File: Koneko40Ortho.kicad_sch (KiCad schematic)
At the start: 24 parts, among them J1 Conn_01x04_MountingPin, J2 TC2030_SWD, SW73 SW_Push, U2 STM32L443CCUx, U4 3.3V Fixed Regulator

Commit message: Aug202023-7:30pm
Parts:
- added JP1: Jumper_2_Open, Connector_PinHeader_1.27mm:PinHeader_1x02_P1.27mm_Vertical, symbol Jumper:Jumper_2_Open
- added R1: 10k 0402, Resistor_SMD:R_0402_1005Metric, symbol Device:R_Small_US
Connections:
- net +3.3V: now also JP1.2 (B)
- net GND: now also R1.2
- net at U2.44 (PH3): now also JP1.1 (A), R1.1

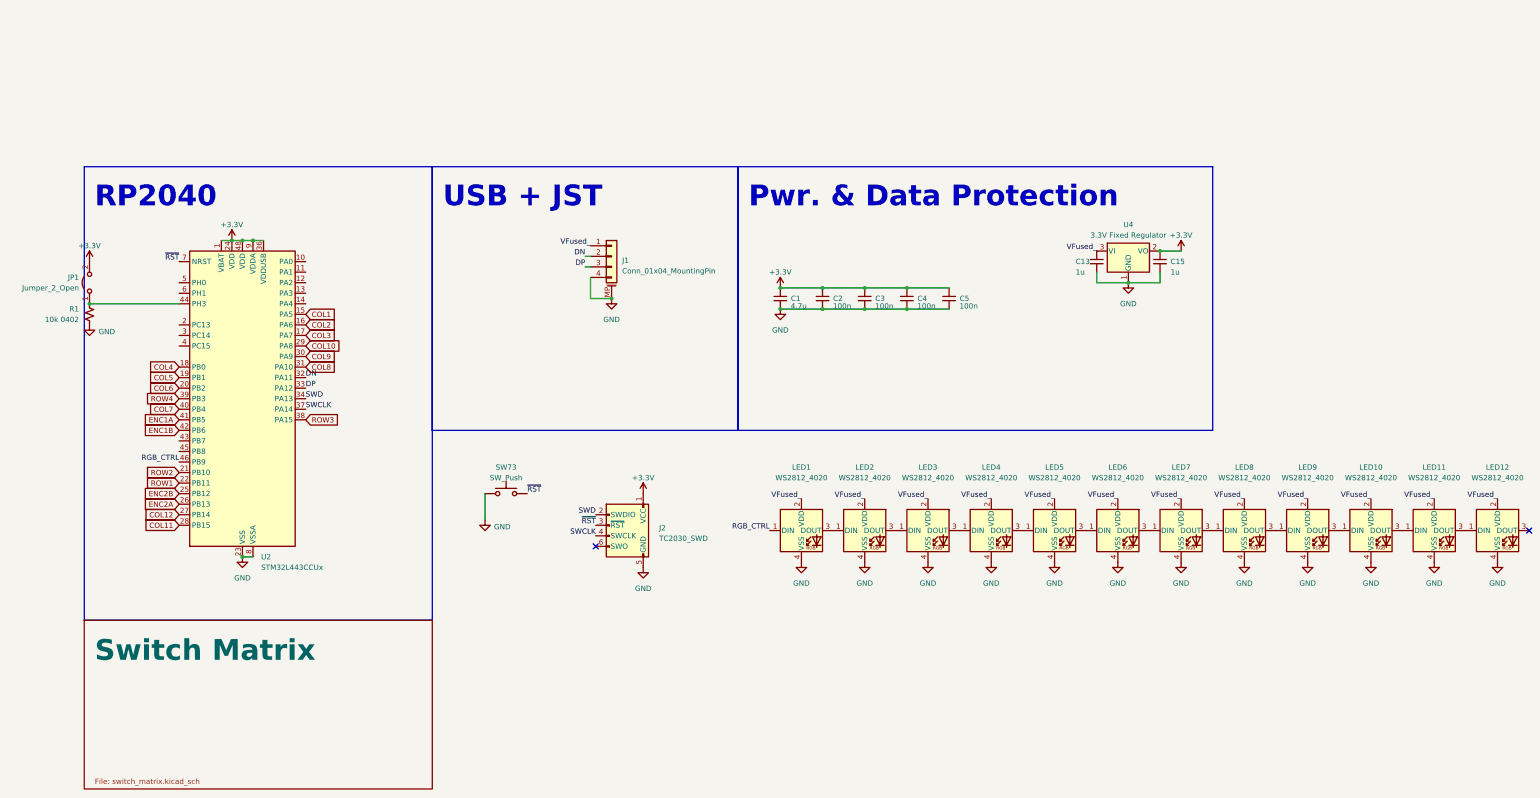
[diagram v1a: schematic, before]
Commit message: Refactored to use RP2040
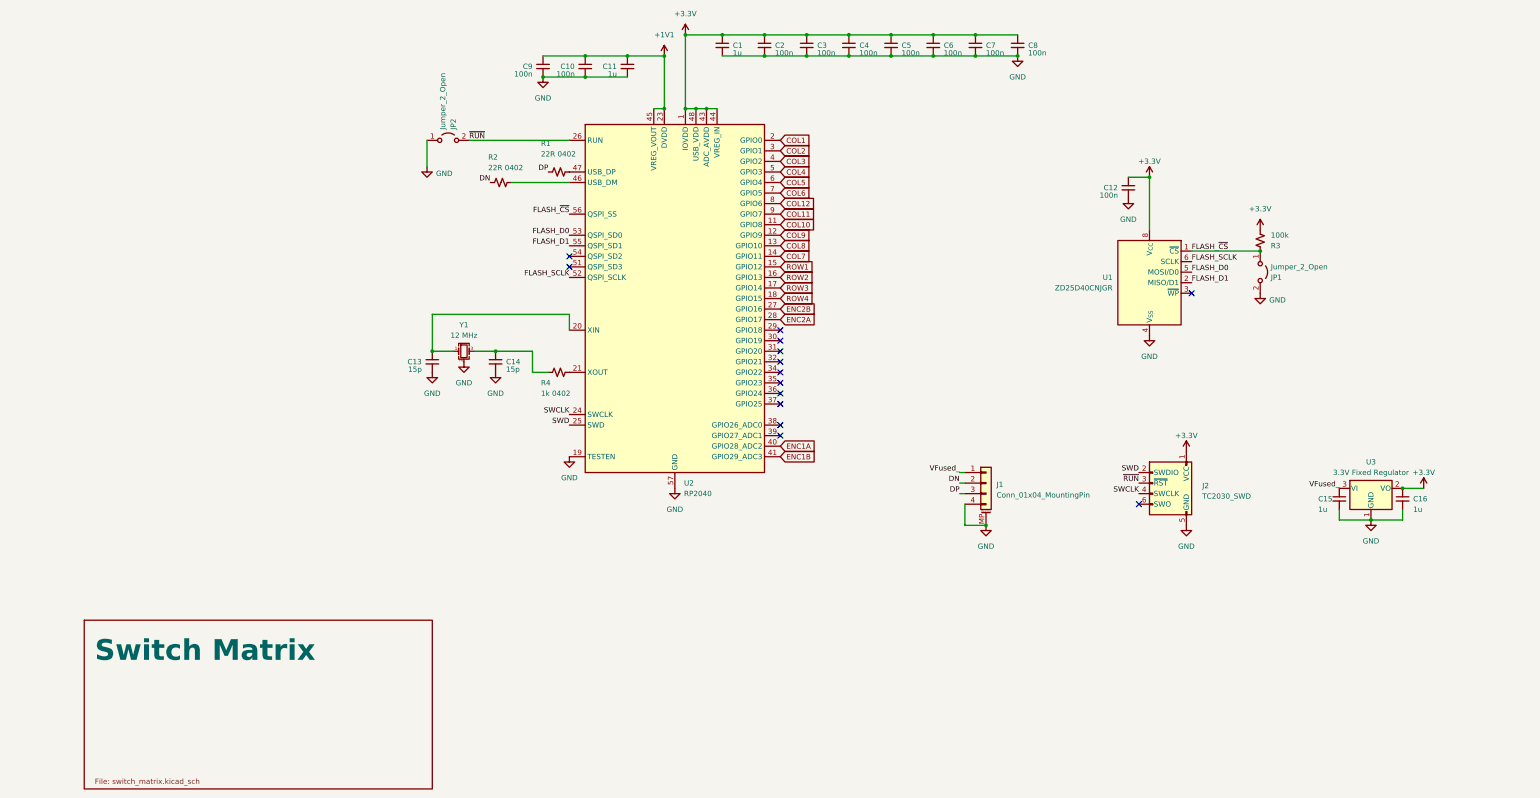
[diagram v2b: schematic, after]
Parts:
- removed LED1, LED10, LED11, LED12, LED2, LED3, LED4, LED5, LED6, LED7, LED8, LED9: WS2812_4020, PCM_marbastlib-xp-various:LED_WS2812_4020, symbol marbastlib-various:WS2812_4020
- removed SW73: SW_Push, Button_Switch_SMD:SW_SPST_SKQG_WithoutStem, symbol Switch:SW_Push
- removed U2: STM32L443CCUx, Package_DFN_QFN:QFN-48-1EP_7x7mm_P0.5mm_EP5.6x5.6mm_ThermalVias, symbol MCU_ST_STM32L4:STM32L443CCUx
- removed U4: 3.3V Fixed Regulator, Package_TO_SOT_SMD:TSOT-23, symbol Regulator_Linear:AP2127N3-1.2
- added C10, C12, C6, C7, C8, C9: 100n, Capacitor_SMD:C_0402_1005Metric, symbol Device:C_Small
- added C11, C16: 1u, Capacitor_SMD:C_0402_1005Metric, symbol Device:C_Small
- added C14: 15p, Capacitor_SMD:C_0402_1005Metric, symbol Device:C_Small
- added JP2: Jumper_2_Open, Connector_PinHeader_1.27mm:PinHeader_1x02_P1.27mm_Vertical, symbol Jumper:Jumper_2_Open
- added R2: 22R 0402, Resistor_SMD:R_0402_1005Metric, symbol Device:R_Small_US
- added R3: 100k, Resistor_SMD:R_0402_1005Metric, symbol Device:R_Small_US
- added R4: 1k 0402, Resistor_SMD:R_0402_1005Metric, symbol Device:R_Small_US
- added U1: ZD25D40CNJGR, USON8:USON-8_1.5x1.5mm_P0.45mm, symbol Flash_NOR_SPI:ZD25D40CNJGR
- added U2: RP2040, Package_DFN_QFN:QFN-56-1EP_7x7mm_P0.4mm_EP3.2x3.2mm, symbol MCU_RaspberryPi:RP2040
- added U3: 3.3V Fixed Regulator, Package_TO_SOT_SMD:TSOT-23, symbol Regulator_Linear:AP2127N3-1.2
- added Y1: 12 MHz, Crystal:Crystal_SMD_2520-4Pin_2.5x2.0mm, symbol EasyCrystal:Crystal_GND24_Small_EZ
- C1: value 4.7u -> 1u; LCSC C52923 -> C318573
- C13: value 1u -> 15p; LCSC C52923 -> C106997
- C15: LCSC C52923 -> C318573
- C2, C3, C4, C5: LCSC C1525 -> C110251
- J1: LCSC C528030 -> C160404
- R1: value 10k 0402 -> 22R 0402; LCSC C60490 -> C25092
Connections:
- net +3.3V: now also C12.1, C16.1, C6.1, C7.1, C8.1, R3.2, U1.8 (V_{CC}), U2.1 (IOVDD), U2.10 (IOVDD), U2.22 (IOVDD), U2.33 (IOVDD), U2.42 (IOVDD), U2.43 (ADC_AVDD), U2.44 (VREG_IN), U2.48 (USB_VDD), U2.49 (IOVDD), U3.2 (VO); no longer C15.1, JP1.2 (B)
- net COL1: now also U2.2 (GPIO0)
- net COL10: now also U2.11 (GPIO8)
- net COL11: now also U2.9 (GPIO7)
- net COL12: now also U2.8 (GPIO6)
- net COL2: now also U2.3 (GPIO1)
- net COL3: now also U2.4 (GPIO2)
- net COL4: now also U2.5 (GPIO3)
- net COL5: now also U2.6 (GPIO4)
- net COL6: now also U2.7 (GPIO5)
- net COL7: now also U2.14 (GPIO11)
- net COL8: now also U2.13 (GPIO10)
- net COL9: now also U2.12 (GPIO9)
- net DN: now also R2.2
- net DP: now also R1.2
- net ENC1A: now also U2.40 (GPIO28_ADC2)
- net ENC1B: now also U2.41 (GPIO29_ADC3)
- net ENC2A: now also U2.28 (GPIO17)
- net ENC2B: now also U2.27 (GPIO16)
- net GND: now also JP1.2 (B), C10.2, C11.2, C12.2, C14.2, C16.2, C6.2, C7.2, C8.2, C9.2, JP2.1 (A), U1.4 (V_{SS}), U1.9 (PAD/V_{SS}), U2.19 (TESTEN), U2.57 (GND), U3.1 (GND), Y1.2, Y1.4; no longer R1.2
- net ROW1: now also U2.15 (GPIO12)
- net ROW2: now also U2.16 (GPIO13)
- net ROW3: now also U2.17 (GPIO14)
- net ROW4: now also U2.18 (GPIO15)
- net SWCLK: now also U2.24 (SWCLK)
- net SWD: now also U2.25 (SWD)
- net VFused_: now also C15.1, U3.3 (VI); no longer C13.1
- net at R1.1: now also U2.47 (USB_DP); no longer JP1.1 (A)
- net ~{RST} renamed ~{RUN}
- net ~{RUN}: now also JP2.2 (B), U2.26 (RUN)
- new net: C14.1, R4.1, Y1.3
- new net: R4.2, U2.21 (XOUT)
- new net: C13.1, U2.20 (XIN), Y1.1
- new net: R2.1, U2.46 (USB_DM)
- new net +1V1: C10.1, C11.1, C9.1, U2.23 (DVDD), U2.45 (VREG_VOUT), U2.50 (DVDD)
- new net FLASH_D0: U1.5 (MOSI/D0), U2.53 (QSPI_SD0)
- new net FLASH_D1: U1.2 (MISO/D1), U2.55 (QSPI_SD1)
- new net FLASH_SCLK: U1.6 (SCLK), U2.52 (QSPI_SCLK)
- new net FLASH_~{CS}: JP1.1 (A), R3.1, U1.1 (~{CS}), U2.56 (QSPI_SS)
- no-connect marks 2 -> 14
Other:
- note removed: "Pwr. & Data Protection"
- note removed: "RP2040"
- note removed: "USB + JST"

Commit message: Fixed resistor part number.
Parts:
- R4: LCSC C60490 -> C11702
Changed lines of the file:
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@@
       (effects (font (size 1.27 1.27)) hide)
     )
-    (property "LCSC" "C60490" (at 127 87.63 0)
+    (property "LCSC" "C11702" (at 127 87.63 0)
       (effects (font (size 1.27 1.27)) hide)
     )
